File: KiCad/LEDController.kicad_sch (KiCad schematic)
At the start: 33 parts, among them J1 Conn_01x05, J2 Power in, J3 LED Power, J4 LED Power, J5 USB_C_Receptacle_USB2.0_16P, J6 Conn_01x03, Q1 IRLZ44N, Q2 IRLZ44N, Q3 IRLZ44N, Q4 IRLZ44N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

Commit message: start routing
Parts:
- added H1, H2, H3, H4: MountingHole, MountingHole:MountingHole_3.2mm_M3, symbol Mechanical:MountingHole
- added JP1: SolderJumper_2_Open, Jumper:SolderJumper-2_P1.3mm_Open_RoundedPad1.0x1.5mm, symbol Jumper:SolderJumper_2_Open
- J1, J2, J3, J4, J6: now not fitted
- Q1, Q2, Q3, Q4: LCSC (none) -> C42370423
- R1, R2, R3, R4, R8: LCSC (none) -> C3017875
- R5, R6, R7: LCSC (none) -> C2930231
- R9: LCSC (none) -> C2907294
- U1: LCSC (none) -> C81563
- U2: LCSC (none) -> C2913198
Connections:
- net +24V: now also JP1.1 (A); no longer J6.1 (Pin_1)
- net 3.3V Switch: now reaches L1.1, U1.1 (SW), U1.2 (SW), U1.3 (SW)
- new net: J6.1 (Pin_1), JP1.2 (B)
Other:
- moved on the sheet: C9, L1, R8, R9

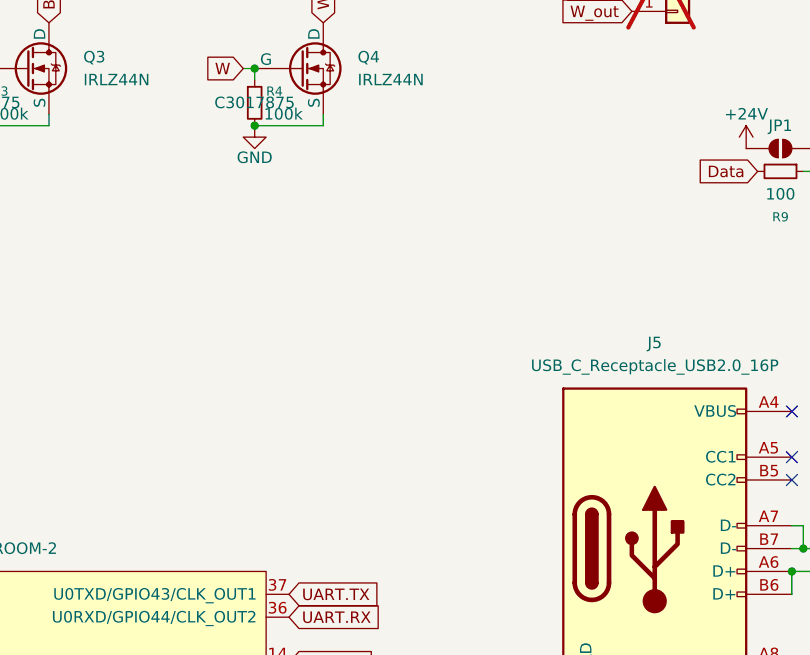
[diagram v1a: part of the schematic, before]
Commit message: add aditional header
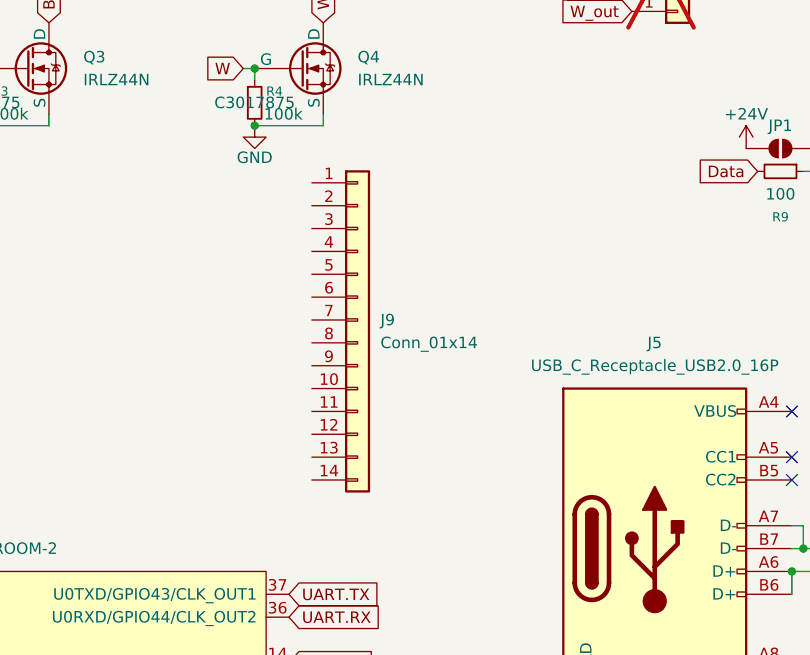
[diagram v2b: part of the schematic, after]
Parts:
- added J9: Conn_01x14, Connector_PinHeader_2.54mm:PinHeader_1x14_P2.54mm_Vertical, symbol Connector_Generic:Conn_01x14
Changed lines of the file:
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@@
 		(polyline
 			(pts
-				(xy 171.45 50.8) (xy 217.17 50.8) (xy 217.17 73.66) (xy 208.28 73.66) (xy 171.45 73.66) (xy 171.45 69.85)
+				(xy 157.48 29.21) (xy 157.48 48.26) (xy 180.34 48.26) (xy 180.34 29.21)
 			)
 			(stroke
@@
 		(length 2.54)
 		(shape round)
-		(at 191.77 50.8 0)
+		(at 171.45 29.21 0)
 		(fields_autoplaced yes)
 		(effects
@@
 		)
 		(property "Netclass" "Power"
-			(at 192.4685 48.26 0)
+			(at 172.1485 26.67 0)
 			(effects
 				(font
@@
 		)
 		(property "Component Class" ""
-			(at -71.12 20.32 0)
+			(at -91.44 -1.27 0)
+			(effects
+				(font
+					(size 1.27 1.27)
+					(italic yes)
+				)
+			)
+		)
+	)
+	(netclass_flag ""
+		(length 2.54)
+		(shape round)
+		(at 189.23 59.69 0)
+		(fields_autoplaced yes)
+		(effects
+			(font
+				(size 1.27 1.27)
+			)
+			(justify left bottom)
+		)
+		(property "Netclass" "Power"
+			(at 189.9285 57.15 0)
+			(effects
+				(font
+					(size 1.27 1.27)
+				)
+				(justify left)
+			)
+		)
+		(property "Component Class" ""
+			(at -73.66 29.21 0)
 			(effects
 				(font
@@
 					(unit 1)
 				)
+			)
+		)
+	)
+	(symbol
+		(lib_id "Connector_Generic:Conn_01x14")
+		(at 137.16 78.74 0)
+		(unit 1)
+		(exclude_from_sim no)
+		(in_bom yes)
+		(on_board yes)
+		(dnp no)
+		(fields_autoplaced yes)
+		(property "Reference" "J9"
+			(at 139.7 78.7399 0)
+			(effects
+				(font
+					(size 1.27 1.27)
+				)
+				(justify left)
+			)
+		)
+		(property "Value" "Conn_01x14"
+			(at 139.7 81.2799 0)
+			(effects
+				(font
+					(size 1.27 1.27)
+				)
+				(justify left)
+			)
+		)
+		(property "Footprint" "Connector_PinHeader_2.54mm:PinHeader_1x14_P2.54mm_Vertical"
+			(at 137.16 78.74 0)
+			(effects
+				(font
+					(size 1.27 1.27)
+				)
+				(hide yes)
+			)
+		)
+		(property "Datasheet" "~"
+			(at 137.16 78.74 0)
+			(effects
+				(font
+					(size 1.27 1.27)
+				)
+				(hide yes)
+			)
+		)
+		(property "Description" "Generic connector, single row, 01x14, script generated (kicad-library-utils/schlib/autogen/connector/)"
+			(at 137.16 78.74 0)
+			(effects
+				(font
+					(size 1.27 1.27)
+				)
+				(hide yes)
+			)
+		)
+		(property "LCSC" ""
+			(at 137.16 78.74 0)
+			(effects
+				(font
+					(size 1.27 1.27)
+				)
+				(hide yes)
+			)
+		)
+		(pin "6"
+		)
+		(pin "2"
+		)
+		(pin "3"
+		)
+		(pin "4"
+		)
+		(pin "5"
+		)
+		(pin "1"
+		)
+		(pin "12"
+		)
+		(pin "13"
+		)
+		(pin "14"
+		)
+		(pin "7"
+		)
+		(pin "10"
+		)
+		(pin "9"
+		)
+		(pin "8"
+		)
+		(pin "11"
+		)
+		(instances
+			(project ""
+				(path "/4e4f96d2-86d5-4a03-8de9-74109a01887a"
+					(reference "J9")
+					(unit 1)
+				)

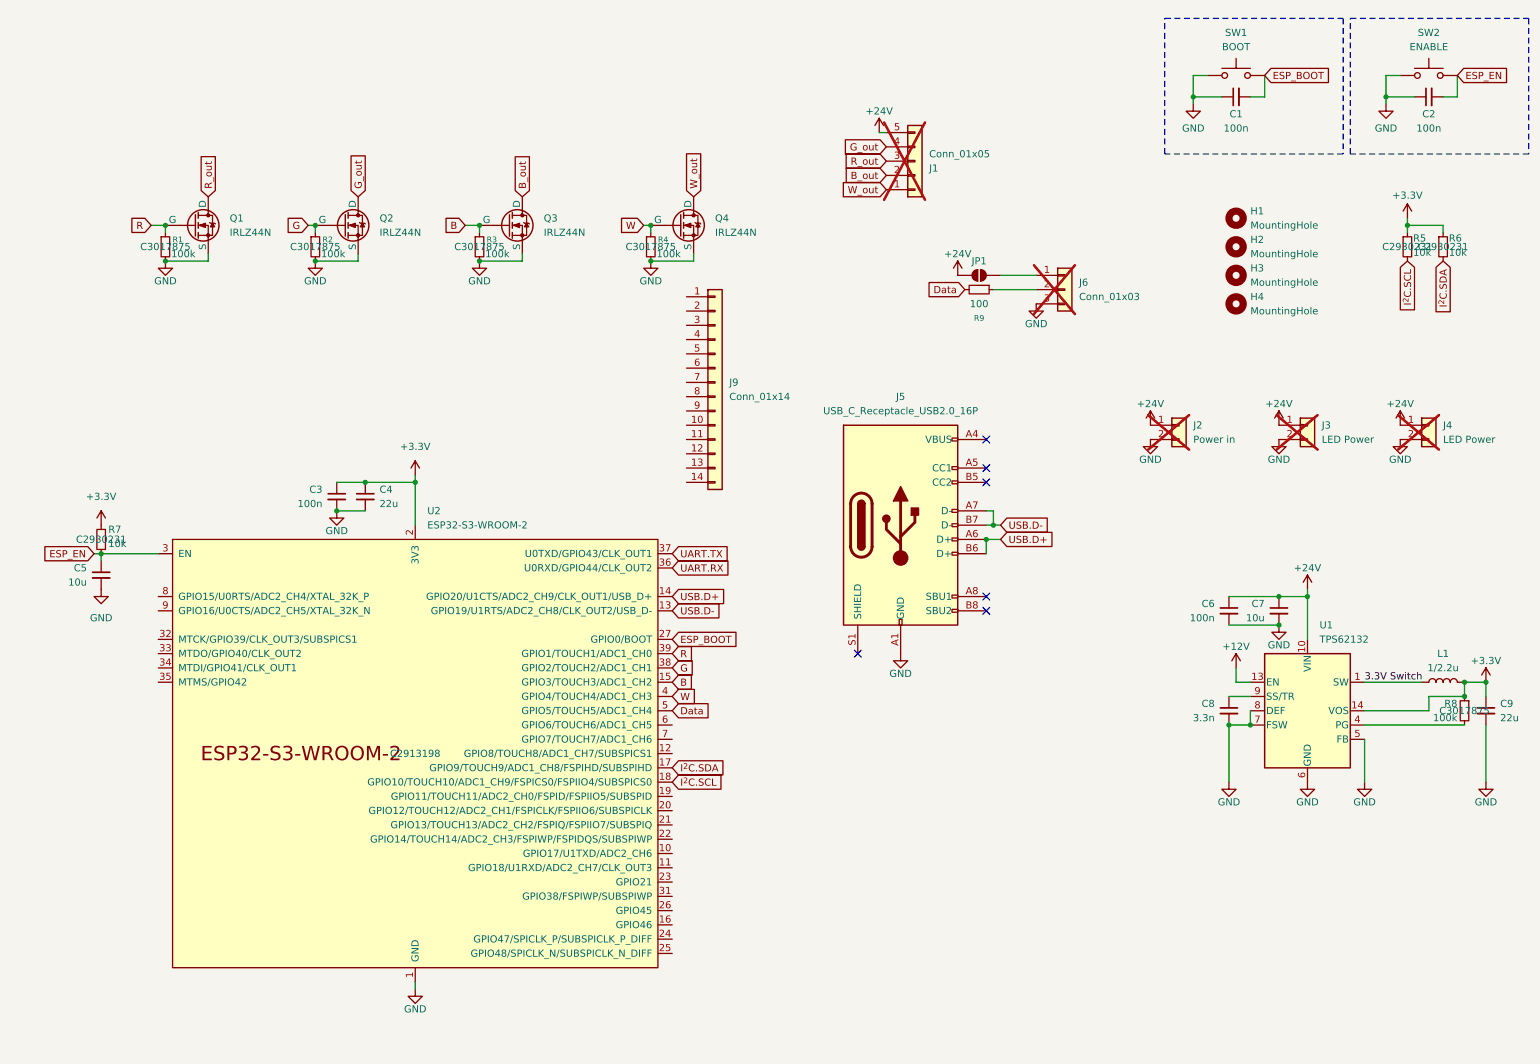
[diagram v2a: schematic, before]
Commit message: add kikit board2pdf, add some headers, route
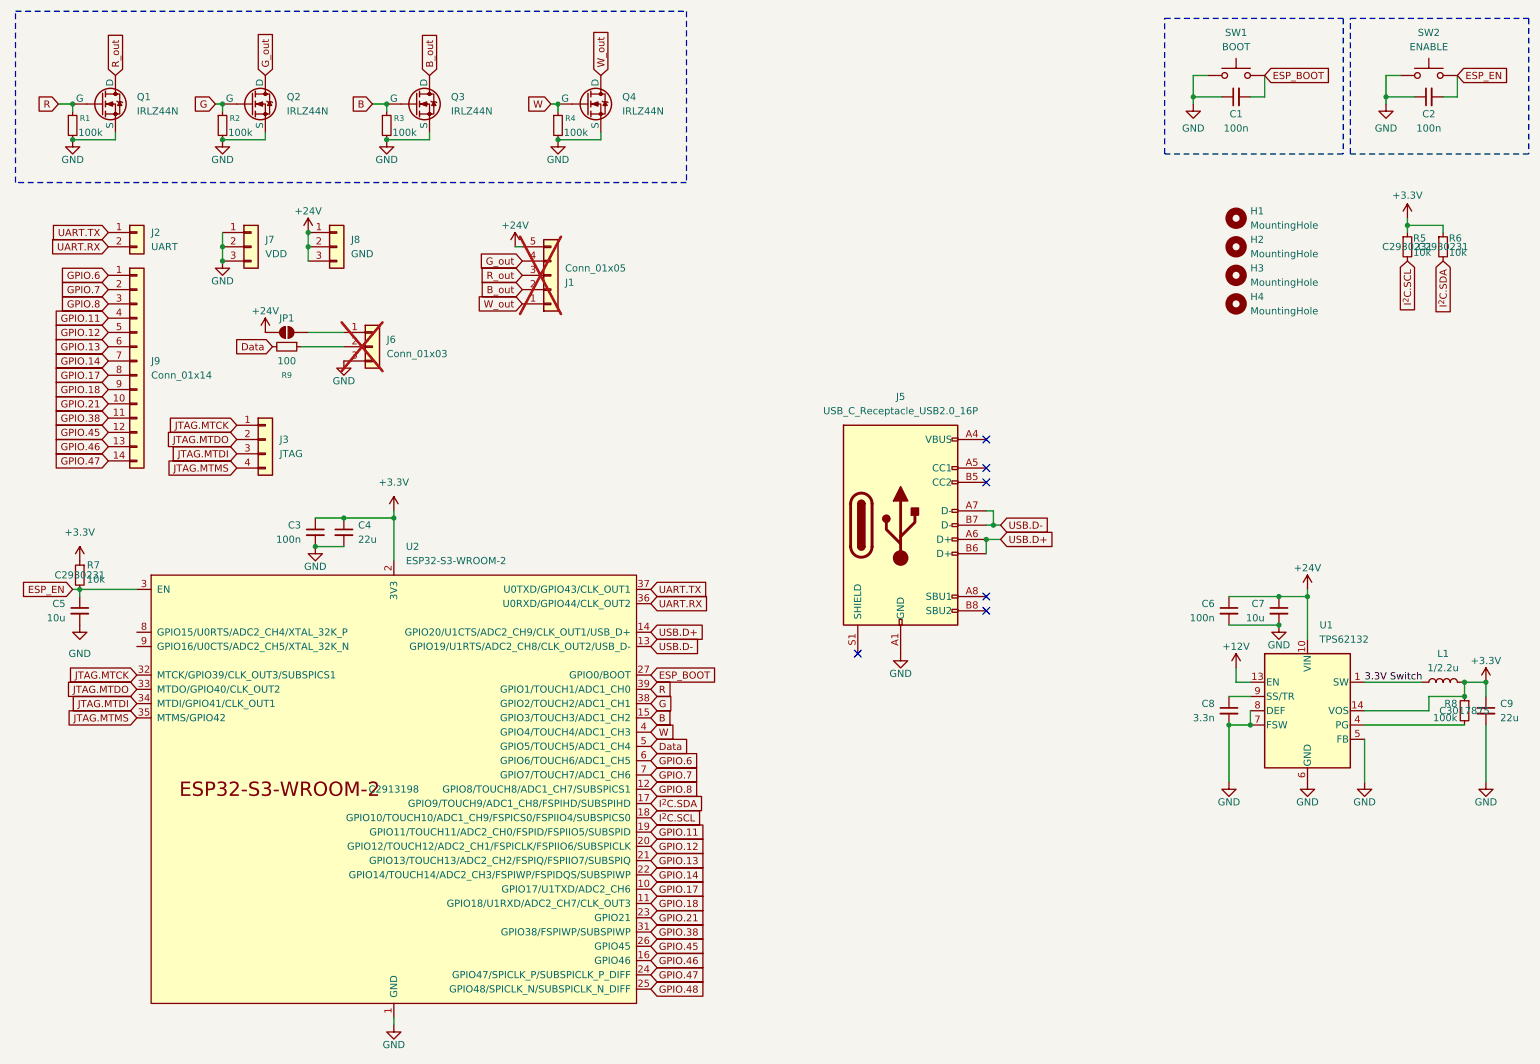
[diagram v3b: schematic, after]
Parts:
- removed J3, J4: LED Power, TerminalBlock_Phoenix:TerminalBlock_Phoenix_MKDS-1,5-2-5.08_1x02_P5.08mm_Horizontal, symbol Connector_Generic:Conn_01x02
- added J3: JTAG, Connector_PinHeader_2.54mm:PinHeader_1x04_P2.54mm_Vertical, symbol Connector_Generic:Conn_01x04
- added J7: VDD, TerminalBlock_Phoenix:TerminalBlock_Phoenix_MKDS-1,5-3-5.08_1x03_P5.08mm_Horizontal, symbol Connector_Generic:Conn_01x03
- added J8: GND, TerminalBlock_Phoenix:TerminalBlock_Phoenix_MKDS-1,5-3-5.08_1x03_P5.08mm_Horizontal, symbol Connector_Generic:Conn_01x03
- J2: value Power in -> UART; footprint TerminalBlock_Phoenix:TerminalBlock_Phoenix_MKDS-1,5-2-5.08_1x02_P5.08mm_Horizontal -> Connector_PinHeader_2.54mm:PinHeader_1x02_P2.54mm_Vertical; now fitted
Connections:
- net +24V: now also J8.1 (Pin_1), J8.2 (Pin_2), J8.3 (Pin_3); no longer J2.1 (Pin_1)
- net GND: now also J7.1 (Pin_1), J7.2 (Pin_2), J7.3 (Pin_3); no longer J2.2 (Pin_2)
- net UART.RX: now also J2.2 (Pin_2)
- net UART.TX: now also J2.1 (Pin_1)
- net GPIO.17: now reaches U2.10 (GPIO17/U1TXD/ADC2_CH6)
- net GPIO.17: now also J9.8 (Pin_8)
- net GPIO.18: now reaches U2.11 (GPIO18/U1RXD/ADC2_CH7/CLK_OUT3)
- net GPIO.18: now also J9.9 (Pin_9)
- net GPIO.8: now reaches U2.12 (GPIO8/TOUCH8/ADC1_CH7/SUBSPICS1)
- net GPIO.8: now also J9.3 (Pin_3)
- net GPIO.46: now reaches U2.16 (GPIO46)
- net GPIO.46: now also J9.13 (Pin_13)
- net GPIO.11: now reaches U2.19 (GPIO11/TOUCH11/ADC2_CH0/FSPID/FSPIIO5/SUBSPID)
- net GPIO.11: now also J9.4 (Pin_4)
- net GPIO.12: now reaches U2.20 (GPIO12/TOUCH12/ADC2_CH1/FSPICLK/FSPIIO6/SUBSPICLK)
- net GPIO.12: now also J9.5 (Pin_5)
- net GPIO.13: now reaches U2.21 (GPIO13/TOUCH13/ADC2_CH2/FSPIQ/FSPIIO7/SUBSPIQ)
- net GPIO.13: now also J9.6 (Pin_6)
- net GPIO.14: now reaches U2.22 (GPIO14/TOUCH14/ADC2_CH3/FSPIWP/FSPIDQS/SUBSPIWP)
- net GPIO.14: now also J9.7 (Pin_7)
- net GPIO.21: now reaches U2.23 (GPIO21)
- net GPIO.21: now also J9.10 (Pin_10)
- net GPIO.47: now reaches U2.24 (GPIO47/SPICLK_P/SUBSPICLK_P_DIFF)
- net GPIO.47: now also J9.14 (Pin_14)
- net GPIO.48: now reaches U2.25 (GPIO48/SPICLK_N/SUBSPICLK_N_DIFF)
- net GPIO.45: now reaches U2.26 (GPIO45)
- net GPIO.45: now also J9.12 (Pin_12)
- net GPIO.38: now reaches U2.31 (GPIO38/FSPIWP/SUBSPIWP)
- net GPIO.38: now also J9.11 (Pin_11)
- net JTAG.MTCK: now reaches U2.32 (MTCK/GPIO39/CLK_OUT3/SUBSPICS1)
- net JTAG.MTCK: now also J3.1 (Pin_1)
- net JTAG.MTDO: now reaches U2.33 (MTDO/GPIO40/CLK_OUT2)
- net JTAG.MTDO: now also J3.2 (Pin_2)
- net JTAG.MTDI: now reaches U2.34 (MTDI/GPIO41/CLK_OUT1)
- net JTAG.MTDI: now also J3.3 (Pin_3)
- net JTAG.MTMS: now reaches U2.35 (MTMS/GPIO42)
- net JTAG.MTMS: now also J3.4 (Pin_4)
- net GPIO.6: now reaches U2.6 (GPIO6/TOUCH6/ADC1_CH5)
- net GPIO.6: now also J9.1 (Pin_1)
- net GPIO.7: now reaches U2.7 (GPIO7/TOUCH7/ADC1_CH6)
- net GPIO.7: now also J9.2 (Pin_2)
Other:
- moved on the sheet: C3, C4, C5, J1, J6, J9, JP1, Q1, Q2, Q3, Q4, R1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

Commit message: route
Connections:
- no-connect marks 6 -> 8
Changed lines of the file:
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@@
 	)
 	(no_connect
+		(at 34.29 125.73)
+	)
+	(no_connect
 		(at 185.42 88.9)
 	)
@@
 	)
 	(no_connect
+		(at 34.29 123.19)
+	)
+	(no_connect
 		(at 185.42 96.52)
 	)
@@
 					(size 1.27 1.27)
 				)
+				(hide yes)
 			)
 		)
@@
 					(size 1.27 1.27)
 				)
+				(hide yes)
 			)
 		)
@@
 					(size 1.27 1.27)
 				)
+				(hide yes)
 			)
 		)
@@
 					(size 1.27 1.27)
 				)
+				(hide yes)
 			)
 		)
